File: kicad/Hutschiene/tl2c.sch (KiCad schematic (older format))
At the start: 37 parts, among them IC101 ATTINY20-X, P101 12VDC, P102 I2C Master, P103 Spare, P104 TPI Header, P105 LED_DRIVER, P106 240VAC, P107 LED_DRIVER, P108 UG, P109 5VDC, P110 EG, P111 OG, SW101 TL3315NF160Q

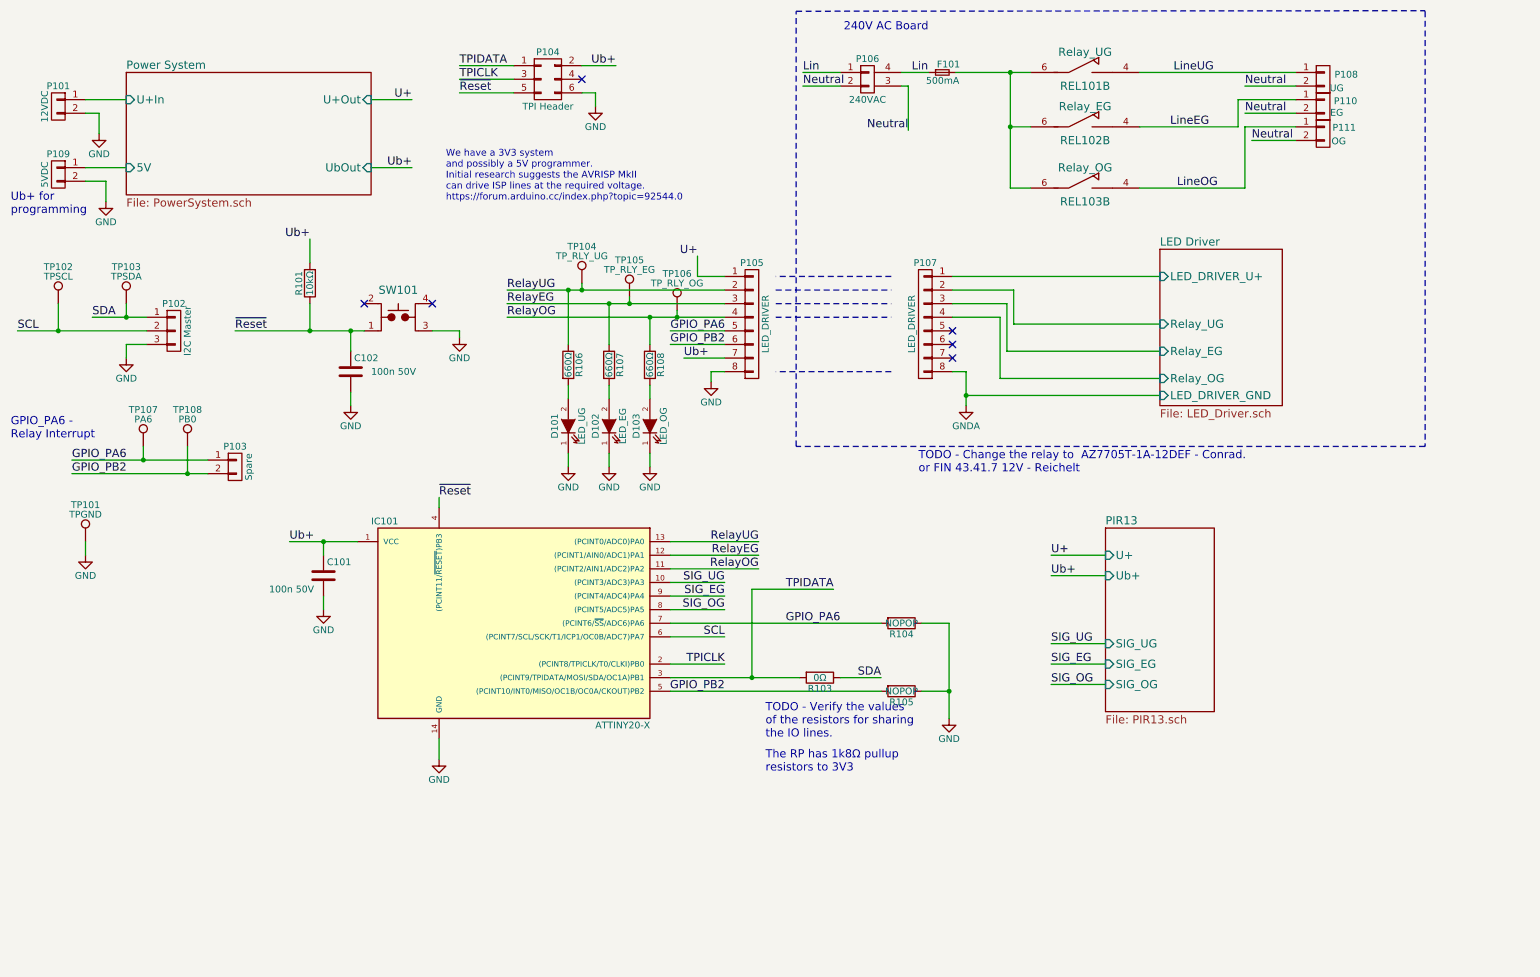
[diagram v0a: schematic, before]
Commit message: Continuing with the Hutschiene design and layout
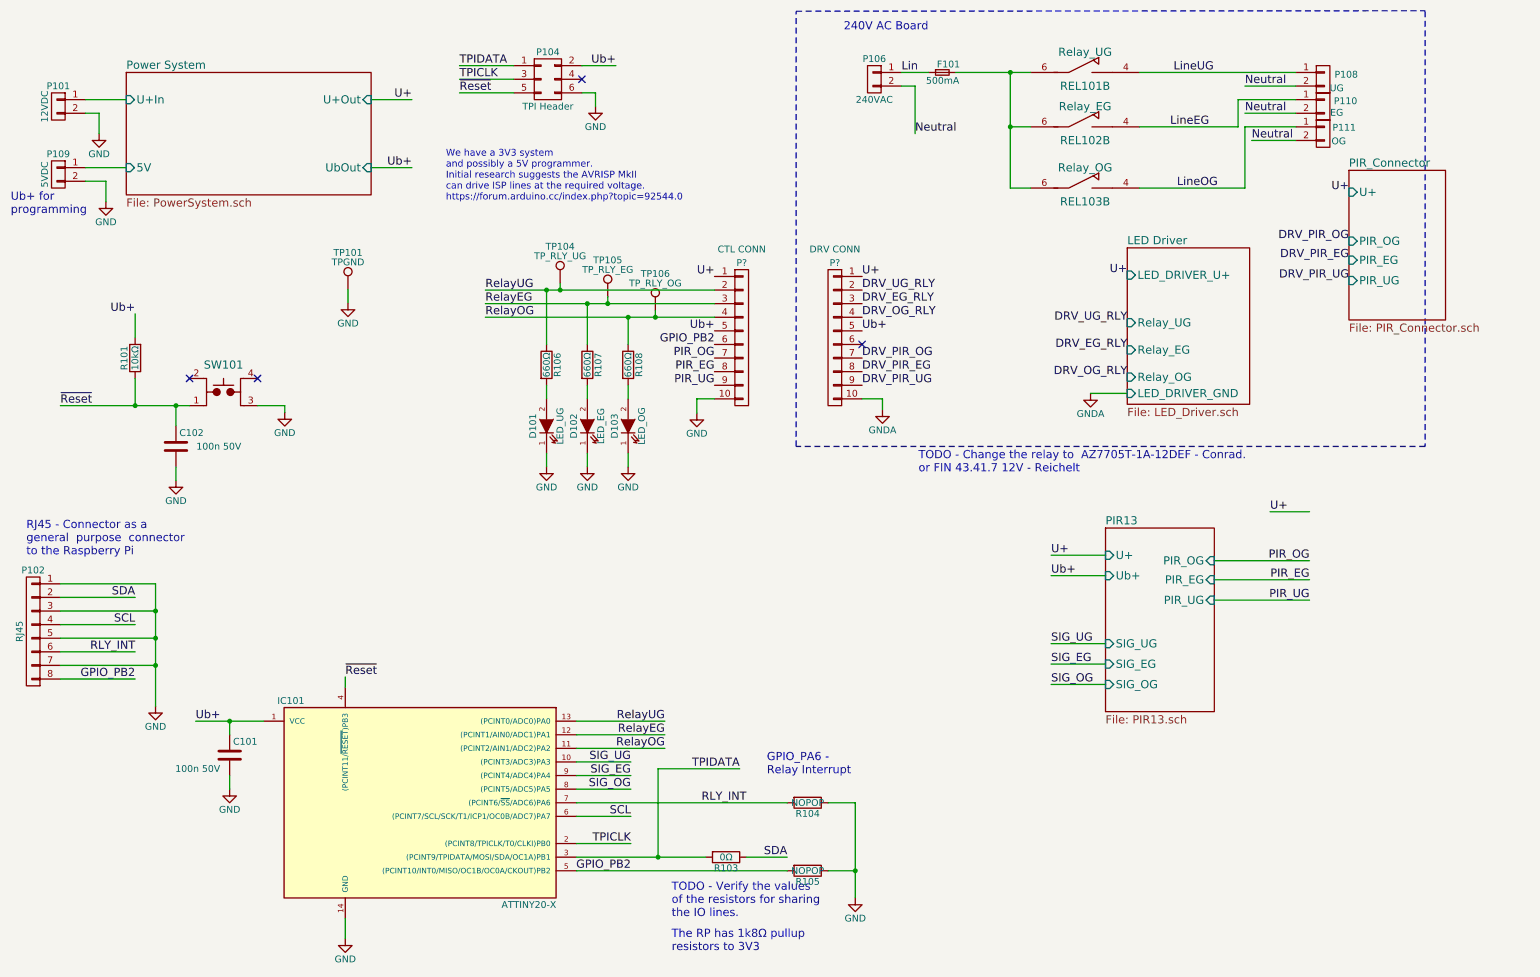
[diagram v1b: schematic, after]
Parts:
- removed P102: I2C Master, tl2c-footprint:Spring_Terminal_Block_1_x_3, symbol CONN_01X03
- removed P103: Spare, Pin_Headers:Pin_Header_Straight_1x02, symbol CONN_01X02
- removed P105, P107: LED_DRIVER, Pin_Headers:Pin_Header_Straight_1x08_Pitch2.54mm, symbol CONN_01X08
- removed P106: 240VAC, tl2c-footprint:PCB_Screw_Terminal_Block_5mm_x_2, symbol Term_01X02
- removed TP102: TPSCL, Measurement_Points:Measurement_Point_Round-SMD-Pad_Small, symbol TEST_1P
- removed TP103: TPSDA, Measurement_Points:Measurement_Point_Round-SMD-Pad_Small, symbol TEST_1P
- removed TP107: PA6, Measurement_Points:Measurement_Point_Round-SMD-Pad_Small, symbol TEST_1P
- removed TP108: PB0, Measurement_Points:Measurement_Point_Round-SMD-Pad_Small, symbol TEST_1P
- added P102: RJ45, Connect:RJ45_8, symbol CONN_01X08
- added P106: 240VAC, tl2c-footprint:PCB_Screw_Terminal_Block_5mm_x_2, symbol CONN_01X02
- added P?: CTL CONN, symbol CONN_01X10
- added P?: DRV CONN, symbol CONN_01X10
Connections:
- net GND: now also P102.1 (P1), P102.3 (P3), P102.5 (P5), P102.7 (P7), P?.10 (P10)
- net GNDA: now also P?.10 (P10)
- net GPIO_PB2: now also P102.8 (P8), P?.6 (P6)
- net Lin: now also P106.1 (P1)
- net Neutral: now also P106.2 (P2)
- net RelayEG: now also P?.3 (P3)
- net RelayOG: now also P?.4 (P4)
- net RelayUG: now also P?.2 (P2)
- net SCL: now also P102.4 (P4)
- net SDA: now also P102.2 (P2)
- net U+: now also P?.1 (P1), P?.1 (P1)
- net Ub+: now also P?.5 (P5), P?.5 (P5)
- net GPIO_PA6 renamed RLY_INT
- net RLY_INT: now also P102.6 (P6)
- new net DRV_EG_RLY: P?.3 (P3)
- new net DRV_OG_RLY: P?.4 (P4)
- new net DRV_PIR_EG: P?.8 (P8)
- new net DRV_PIR_OG: P?.7 (P7)
- new net DRV_PIR_UG: P?.9 (P9)
- new net DRV_UG_RLY: P?.2 (P2)
- new net PIR_EG: P?.8 (P8)
- new net PIR_OG: P?.7 (P7)
- new net PIR_UG: P?.9 (P9)
- no-connect marks 6 -> 4
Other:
- note added: "RJ45 - Connector as a \ngeneral purpose connector \nto the Raspberry Pi"
- moved on the sheet: C101, C102, D101, D102, D103, IC101, R101, R103, R104, R105, R106, R107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

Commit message: Further work on the redesign
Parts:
- P101: footprint Pin_Headers:Pin_Header_Straight_1x02 -> tl2c-footprint:PCB_Screw_Terminal_Block_5mm_x_2
- P103, P105: renamed from P?; footprint (none) -> Pin_Headers:Pin_Header_Straight_2x05_Pitch2.54mm
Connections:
- net U+: no longer P105.1 (P1)
- new net LED Driver/LED_DRIVER_U+: P105.1 (P1)
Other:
- moved on the sheet: D101, D102, D103, F101, P103, P105, P106, P108, P110, P111, R106, R107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

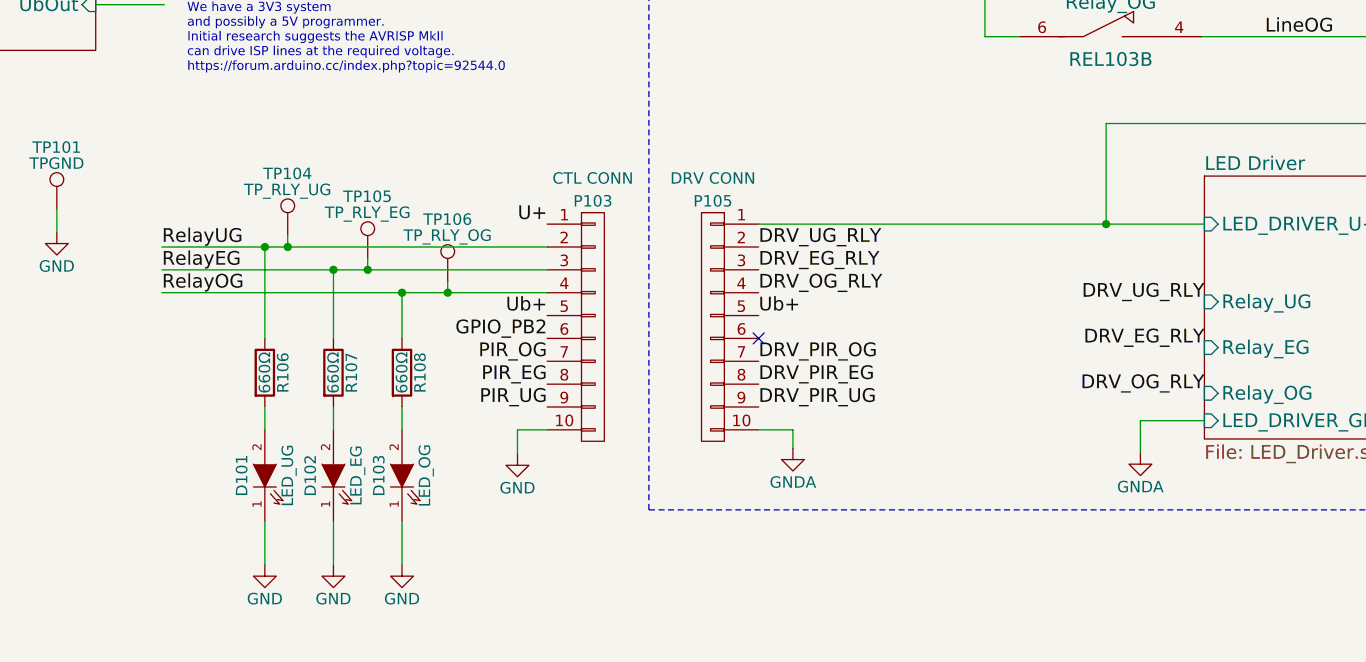
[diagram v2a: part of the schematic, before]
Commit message: Further work on the new Hutschiene Layout
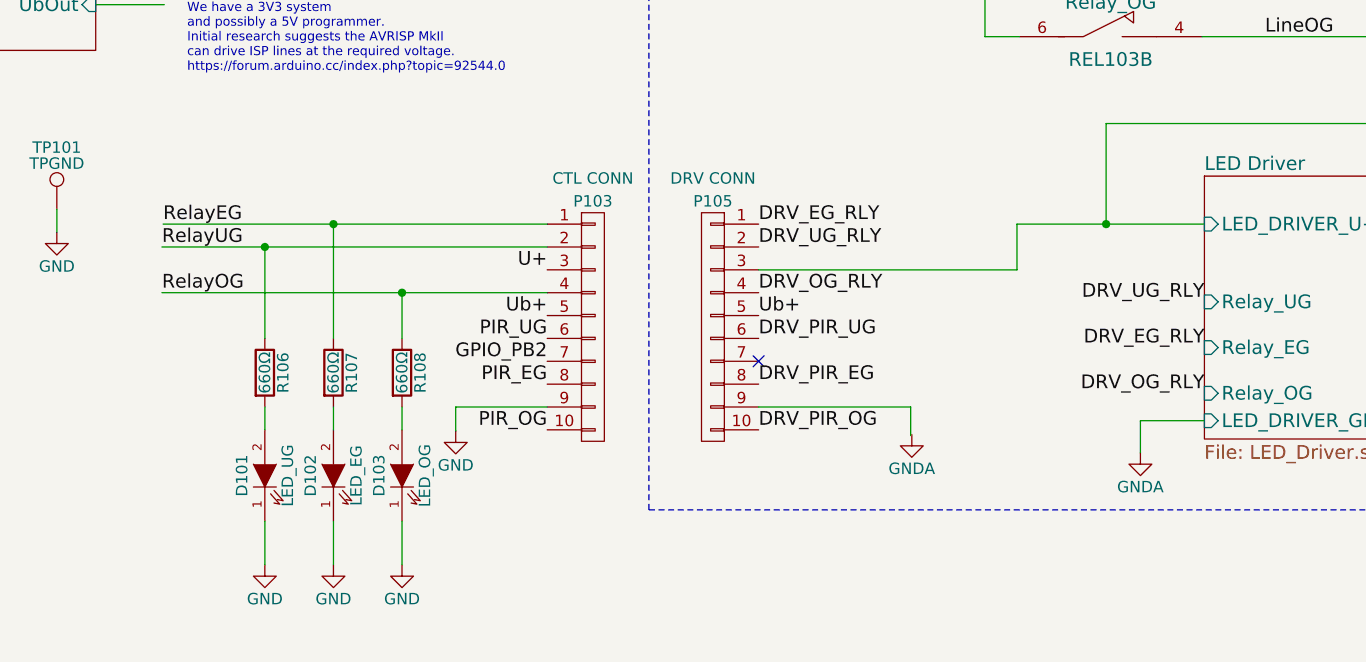
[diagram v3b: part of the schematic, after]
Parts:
- removed TP104: TP_RLY_UG, Measurement_Points:Measurement_Point_Round-SMD-Pad_Small, symbol TEST_1P
- removed TP105: TP_RLY_EG, Measurement_Points:Measurement_Point_Round-SMD-Pad_Small, symbol TEST_1P
- removed TP106: TP_RLY_OG, Measurement_Points:Measurement_Point_Round-SMD-Pad_Small, symbol TEST_1P
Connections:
- net DRV_EG_RLY: now also P105.1 (P1); no longer P105.3 (P3)
- net DRV_PIR_OG: now also P105.10 (P10); no longer P105.7 (P7)
- net DRV_PIR_UG: now also P105.6 (P6); no longer P105.9 (P9)
- net GND: now also P103.9 (P9); no longer P103.10 (P10)
- net GNDA: no longer P105.10 (P10)
- net GPIO_PB2: now also P103.7 (P7); no longer P103.6 (P6)
- net LED Driver/LED_DRIVER_U+: now also P105.3 (P3); no longer P105.1 (P1)
- net PIR_OG: now also P103.10 (P10); no longer P103.7 (P7)
- net PIR_UG: now also P103.6 (P6); no longer P103.9 (P9)
- net RelayEG: now also P103.1 (P1); no longer P103.3 (P3)
- net U+: now also P103.3 (P3); no longer P103.1 (P1)
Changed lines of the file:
@@
 Text Label 3490 2910 0    60   ~ 0
 RelayUG
-Text Label 3490 3010 0    60   ~ 0
+Text Label 3495 2810 0    60   ~ 0
 RelayEG
 Text Label 3490 3110 0    60   ~ 0
@@
 L GNDA #PWR011
 U 1 1 5856E00B
-P 6250 3790
-F 0 "#PWR011" H 6250 3540 50  0001 C CNN
-F 1 "GNDA" H 6250 3640 50  0000 C CNN
-F 2 "" H 6250 3790 50  0000 C CNN
-F 3 "" H 6250 3790 50  0000 C CNN
-	1    6250 3790
+P 6770 3730
+F 0 "#PWR011" H 6770 3480 50  0001 C CNN
+F 1 "GNDA" H 6770 3580 50  0000 C CNN
+F 2 "" H 6770 3730 50  0000 C CNN
+F 3 "" H 6770 3730 50  0000 C CNN
+	1    6770 3730
 	-1   0    0    -1
-$EndComp
-$Comp
-L TEST_1P TP104
-U 1 1 58571150
-P 4040 2860
-F 0 "TP104" H 4040 3130 50  0000 C CNN
-F 1 "TP_RLY_UG" H 4040 3060 50  0000 C CNN
-F 2 "Measurement_Points:Measurement_Point_Round-SMD-Pad_Small" H 4240 2860 50  0001 C CNN
-F 3 "" H 4240 2860 50  0000 C CNN
-	1    4040 2860
-	1    0    0    -1
-$EndComp
-$Comp
-L TEST_1P TP105
-U 1 1 5857134A
-P 4390 2960
-F 0 "TP105" H 4390 3230 50  0000 C CNN
-F 1 "TP_RLY_EG" H 4390 3160 50  0000 C CNN
-F 2 "Measurement_Points:Measurement_Point_Round-SMD-Pad_Small" H 4590 2960 50  0001 C CNN
-F 3 "" H 4590 2960 50  0000 C CNN
-	1    4390 2960
-	1    0    0    -1
-$EndComp
-$Comp
-L TEST_1P TP106
-U 1 1 585714D0
-P 4740 3060
-F 0 "TP106" H 4740 3330 50  0000 C CNN
-F 1 "TP_RLY_OG" H 4740 3260 50  0000 C CNN
-F 2 "Measurement_Points:Measurement_Point_Round-SMD-Pad_Small" H 4940 3060 50  0001 C CNN
-F 3 "" H 4940 3060 50  0000 C CNN
-	1    4740 3060
-	1    0    0    -1
 $EndComp
 Text Notes 9200 3880 0    40   ~ 0
 TODO - Change the relay to  AZ7705T-1A-12DEF - Conrad.\nor FIN 43.41.7 12V - Reichelt
-Text Label 5175 2810 2    60   ~ 0
+Text Label 5175 3010 2    60   ~ 0
 U+
 Text Label 6390 1590 0    60   ~ 0
@@
 Text Label 5175 3210 2    60   ~ 0
 Ub+
-Text Label 5175 3310 2    60   ~ 0
+Text Label 5175 3410 2    60   ~ 0
 GPIO_PB2
 NoConn ~ 4750 1200
@@
 	4710 6120 5360 6120
 Wire Wire Line
-	3490 2910 5175 2910
-Wire Wire Line
-	3490 3010 5175 3010
-Wire Wire Line
 	3490 3110 5175 3110
 Wire Wire Line
 	3940 3310 3940 2910
-Connection ~ 3940 2910
-Wire Wire Line
-	4240 3310 4240 3010
-Connection ~ 4240 3010
+Wire Wire Line
+	4240 2810 4240 3310
 Wire Wire Line
 	4540 3310 4540 3110
 Connection ~ 4540 3110
-Wire Wire Line
-	4040 2860 4040 2910
-Connection ~ 4040 2910
-Wire Wire Line
-	4390 2960 4390 3010
-Connection ~ 4390 3010
-Wire Wire Line
-	4740 3060 4740 3110
-Connection ~ 4740 3110
 Wire Wire Line
 	915  3600 1865 3600
@@
 Text Label 8050 3150 2    60   ~ 0
 DRV_UG_RLY
-Text Label 6100 3010 0    60   ~ 0
+Text Label 6100 2810 0    60   ~ 0
 DRV_EG_RLY
 Text Label 6100 3110 0    60   ~ 0
@@
 F5 "U+" I L 9640 2370 60
 $EndSheet
-Text Label 6100 3410 0    60   ~ 0
+Text Label 6100 3710 0    60   ~ 0
 DRV_PIR_OG
 Text Label 6100 3510 0    60   ~ 0
 DRV_PIR_EG
-Text Label 6100 3610 0    60   ~ 0
+Text Label 6100 3310 0    60   ~ 0
 DRV_PIR_UG
-Text Label 5175 3410 2    60   ~ 0
+Text Label 5175 3710 2    60   ~ 0
 PIR_OG
 Text Label 5175 3510 2    60   ~ 0
 PIR_EG
-Text Label 5175 3610 2    60   ~ 0
+Text Label 5175 3310 2    60   ~ 0
 PIR_UG
 Text Label 9640 2730 2    60   ~ 0
@@
 L GND #PWR016
 U 1 1 596DB6E6
-P 5045 3815
-F 0 "#PWR016" H 5045 3565 50  0001 C CNN
-F 1 "GND" H 5045 3665 50  0000 C CNN
-F 2 "" H 5045 3815 50  0000 C CNN
-F 3 "" H 5045 3815 50  0000 C CNN
-	1    5045 3815
-	1    0    0    -1
-$EndComp
-Wire Wire Line
-	5175 3710 5045 3710
-Wire Wire Line
-	5045 3710 5045 3815
+P 4775 3715
+F 0 "#PWR016" H 4775 3465 50  0001 C CNN
+F 1 "GND" H 4775 3565 50  0000 C CNN
+F 2 "" H 4775 3715 50  0000 C CNN
+F 3 "" H 4775 3715 50  0000 C CNN
+	1    4775 3715
+	1    0    0    -1
+$EndComp
 $Comp
 L CONN_01X10 P105
@@
 Text Label 6100 3210 0    60   ~ 0
 Ub+
-Wire Wire Line
-	6100 3710 6250 3710
-Wire Wire Line
-	6250 3710 6250 3790
-NoConn ~ 6100 3310
-Wire Wire Line
-	6100 2810 8050 2810
+NoConn ~ 6100 3410
+Wire Wire Line
+	7230 2810 8050 2810
 Wire Notes Line
 	5620 720  10950 720
@@
 Wire Wire Line
 	7620 2370 7620 2810
-Connection ~ 7620 2810
 Wire Notes Line
 	10960 4060 10960 720
@@
 Wire Notes Line
 	5620 4060 5620 720
+Wire Wire Line
+	4775 3715 4775 3610
+Wire Wire Line
+	4775 3610 5175 3610
+Wire Wire Line
+	6765 3735 6765 3610
+Wire Wire Line
+	6765 3610 6100 3610
+Connection ~ 3940 2910
+Wire Wire Line
+	3490 2910 5175 2910
+Wire Wire Line
+	3495 2810 5175 2810
+Connection ~ 4240 2810
+Wire Wire Line
+	7230 2810 7230 3010
+Wire Wire Line
+	7230 3010 6100 3010
+Connection ~ 7620 2810
 $EndSCHEMATC
